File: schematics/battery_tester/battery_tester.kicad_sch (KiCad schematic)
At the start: 39 parts, among them J1 BATT1 (AA), J101 XIAO_LEFT, J102 XIAO_RIGHT, J103 ADS1115_1, J104 ADS1115_2, J105 LED_STRIP, J2 BATT2 (AA), J3 BATT3 (AA), J4 BATT4 (AA), J5 BATT5 (AAA)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

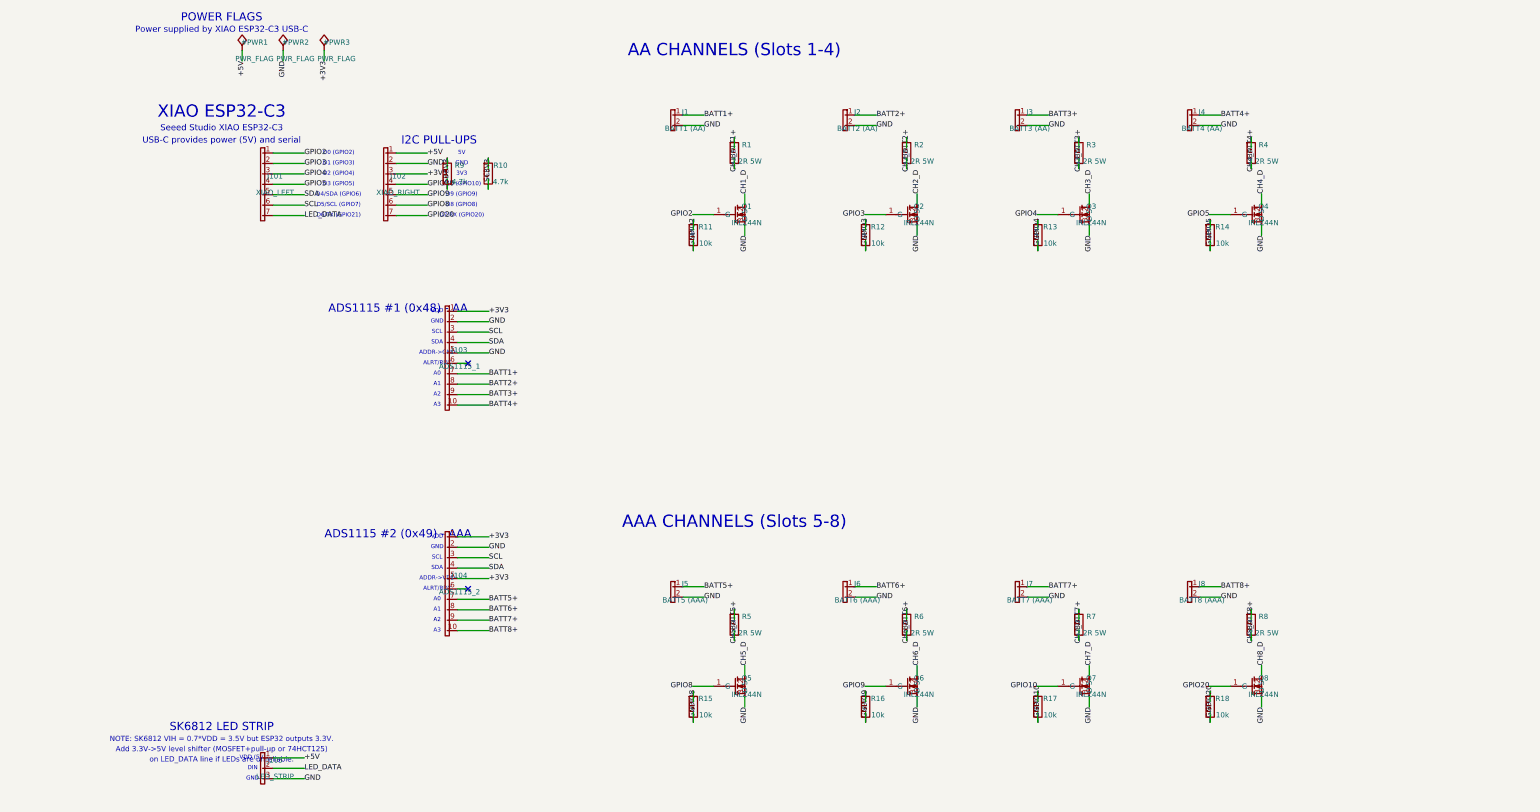
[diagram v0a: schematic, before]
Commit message: Update battery tester hardware and LED logic
Major revision to KiCad schematics and PCB layout (v2.0). Refines LED
behavior by reducing brightness, removing flashing for weak batteries in
favor of a solid color, and wrapping LED writes in a critical section.
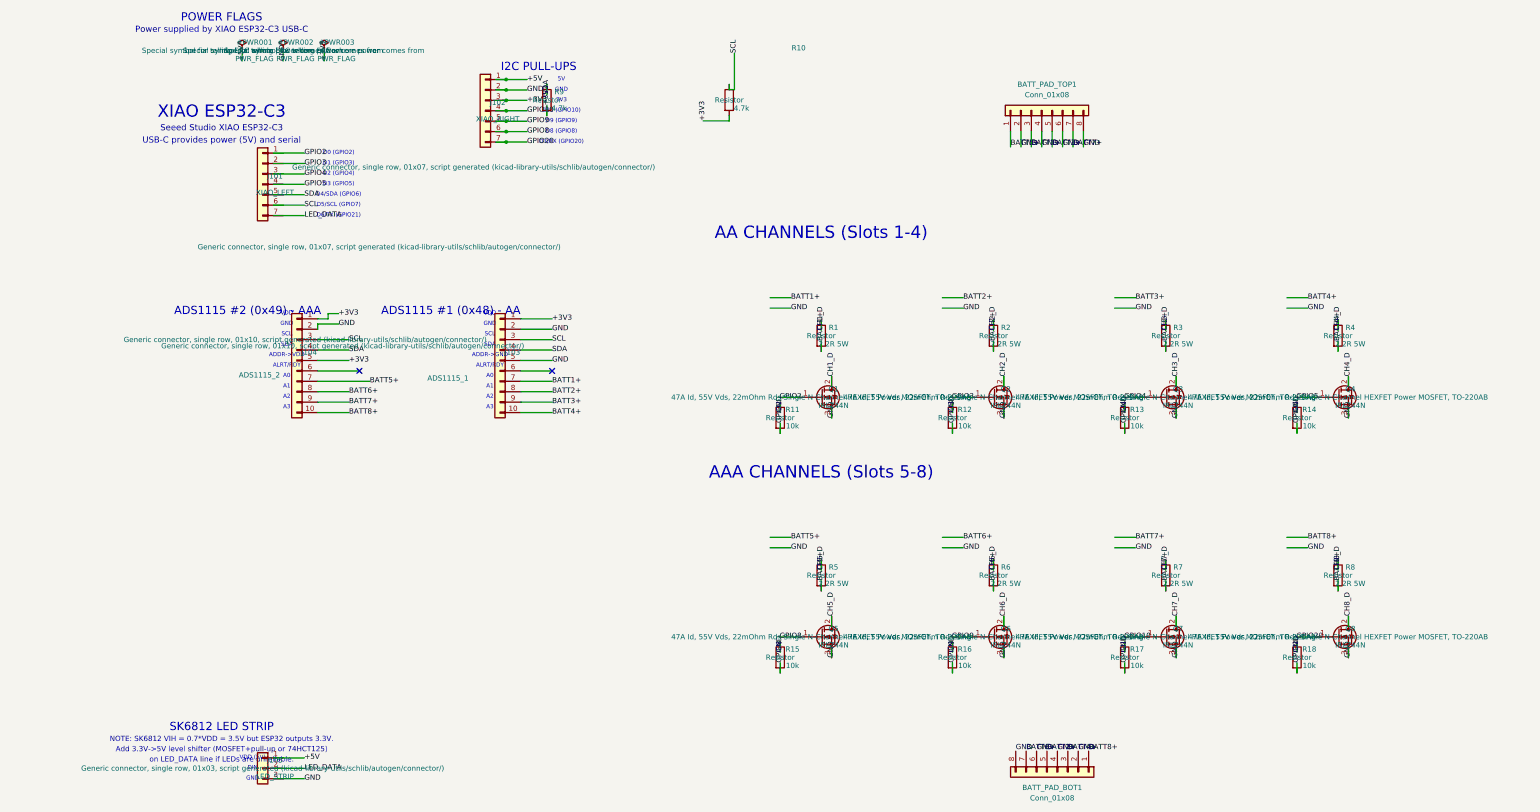
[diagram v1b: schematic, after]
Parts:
- removed J1: BATT1 (AA), symbol Connector_Generic:Conn_01x02
- removed J2: BATT2 (AA), symbol Connector_Generic:Conn_01x02
- removed J3: BATT3 (AA), symbol Connector_Generic:Conn_01x02
- removed J4: BATT4 (AA), symbol Connector_Generic:Conn_01x02
- removed J5: BATT5 (AAA), symbol Connector_Generic:Conn_01x02
- removed J6: BATT6 (AAA), symbol Connector_Generic:Conn_01x02
- removed J7: BATT7 (AAA), symbol Connector_Generic:Conn_01x02
- removed J8: BATT8 (AAA), symbol Connector_Generic:Conn_01x02
- added BATT_PAD_BOT1, BATT_PAD_TOP1: Conn_01x08, Connector_PinHeader_2.54mm:PinHeader_1x08_P2.54mm_Vertical, symbol Connector_Generic:Conn_01x08
- Q1, Q2, Q3, Q4, Q5, Q6, Q7, Q8: footprint (none) -> Package_TO_SOT_THT:TO-220-3_Vertical
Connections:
- net +5V: no longer J105.1 (Pin_1)
- net BATT1+: now also BATT_PAD_TOP1.3 (Pin_3)
- net BATT2+: now also BATT_PAD_BOT1.5 (Pin_5)
- net BATT3+: now also BATT_PAD_TOP1.5 (Pin_5)
- net BATT4+: now also BATT_PAD_BOT1.3 (Pin_3)
- net BATT5+: now also BATT_PAD_TOP1.1 (Pin_1)
- net BATT6+: now also BATT_PAD_BOT1.7 (Pin_7)
- net BATT7+: now also BATT_PAD_TOP1.7 (Pin_7)
- net BATT8+: now also BATT_PAD_BOT1.1 (Pin_1)
- net GND: now also BATT_PAD_BOT1.2 (Pin_2), BATT_PAD_BOT1.4 (Pin_4), BATT_PAD_BOT1.6 (Pin_6), BATT_PAD_BOT1.8 (Pin_8), BATT_PAD_TOP1.2 (Pin_2), BATT_PAD_TOP1.4 (Pin_4), BATT_PAD_TOP1.6 (Pin_6), BATT_PAD_TOP1.8 (Pin_8); no longer J105.3 (Pin_3)
- net GPIO2: no longer J101.1 (Pin_1)
- net GPIO3: no longer J101.2 (Pin_2)
- net GPIO4: no longer J101.3 (Pin_3)
- net GPIO5: no longer J101.4 (Pin_4)
- net LED_DATA: no longer J101.7 (Pin_7), J105.2 (Pin_2)
- net SCL: no longer J101.6 (Pin_6)
- net SDA: no longer J101.5 (Pin_5)
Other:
- moved on the sheet: R1, R10, R11, R12, R13, R14, R15, R16, R17, R18, R2, R3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
